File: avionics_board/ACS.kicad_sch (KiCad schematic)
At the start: 5 parts, among them J1 Conn_02x02_Odd_Even, J2 Conn_02x02_Odd_Even, J3 Conn_02x02_Odd_Even, J4 Conn_02x02_Odd_Even

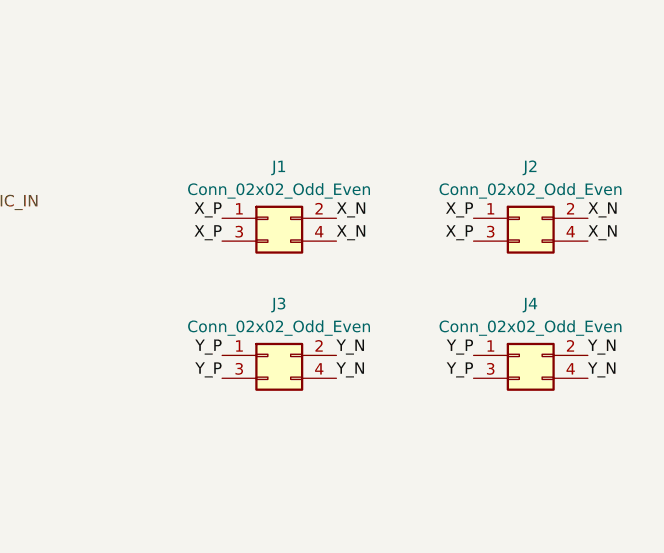
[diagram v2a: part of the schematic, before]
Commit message: AVI: using through hole M50 connectors for sun detectors and ACS
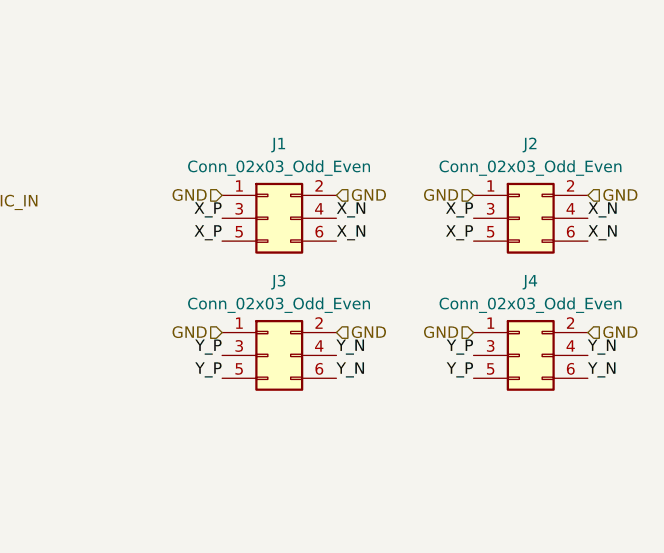
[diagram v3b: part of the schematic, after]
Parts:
- J1, J2, J3, J4: value Conn_02x02_Odd_Even -> Conn_02x03_Odd_Even; footprint Common:SAMTEC-CLP-102-02-X-DH -> Common:HARWIN_M50-3200345; symbol Connector_Generic:Conn_02x02_Odd_Even -> Connector_Generic:Conn_02x03_Odd_Even; Manufacturer (none) -> Harwin; Part Number (none) -> M50-3200345
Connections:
- net GND: now also J1.1 (Pin_1), J1.2 (Pin_2), J2.1 (Pin_1), J2.2 (Pin_2), J3.1 (Pin_1), J3.2 (Pin_2), J4.1 (Pin_1), J4.2 (Pin_2)
- net X_N: now also J1.6 (Pin_6), J2.6 (Pin_6); no longer J1.2 (Pin_2), J2.2 (Pin_2)
- net X_P: now also J1.5 (Pin_5), J2.5 (Pin_5); no longer J1.1 (Pin_1), J2.1 (Pin_1)
- net Y_N: now also J3.6 (Pin_6), J4.6 (Pin_6); no longer J3.2 (Pin_2), J4.2 (Pin_2)
- net Y_P: now also J3.5 (Pin_5), J4.5 (Pin_5); no longer J3.1 (Pin_1), J4.1 (Pin_1)
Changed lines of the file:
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@@
+		)
+	)
+	(hierarchical_label "GND"
+		(shape input)
+		(at 164.465 60.325 0)
+		(fields_autoplaced yes)
+		(effects
+			(font
+				(size 1.27 1.27)
+			)
+			(justify left)
 		)
 	)
@@
 		)
 	)
+	(hierarchical_label "GND"
+		(shape input)
+		(at 192.405 75.565 0)
+		(fields_autoplaced yes)
+		(effects
+			(font
+				(size 1.27 1.27)
+			)
+			(justify left)
+		)
+	)
 	(hierarchical_label "PWR_LOGIC_IN"
 		(shape input)
@@
 	(hierarchical_label "GND"
 		(shape input)
+		(at 151.765 75.565 180)
+		(fields_autoplaced yes)
+		(effects
+			(font
+				(size 1.27 1.27)
+			)
+			(justify right)
+		)
+	)
+	(hierarchical_label "GND"
+		(shape input)
+		(at 151.765 60.325 180)
+		(fields_autoplaced yes)
+		(effects
+			(font
+				(size 1.27 1.27)
+			)
+			(justify right)
+		)
+	)
+	(hierarchical_label "GND"
+		(shape input)
 		(at 71.12 71.755 180)
 		(fields_autoplaced yes)
@@
 		)
 	)
+	(hierarchical_label "GND"
+		(shape input)
+		(at 179.705 60.325 180)
+		(fields_autoplaced yes)
+		(effects
+			(font
+				(size 1.27 1.27)
+			)
+			(justify right)
+		)
+	)
 	(hierarchical_label "Z_PH"
 		(shape input)
@@
 		)
 	)
+	(hierarchical_label "GND"
+		(shape input)
+		(at 179.705 75.565 180)
+		(fields_autoplaced yes)
+		(effects
+			(font
+				(size 1.27 1.27)
+			)
+			(justify right)
+		)
+	)
 	(hierarchical_label "*ACS_INT"
 		(shape input)
@@
 		)
 	)
+	(hierarchical_label "GND"
+		(shape input)
+		(at 164.465 75.565 0)
+		(fields_autoplaced yes)
+		(effects
+			(font
+				(size 1.27 1.27)
+			)
+			(justify left)
+		)
+	)
 	(hierarchical_label "PWR_COIL_IN"
 		(shape input)
@@
 	(hierarchical_label "GND"
 		(shape input)
+		(at 192.405 60.325 0)
+		(fields_autoplaced yes)
+		(effects
+			(font
+				(size 1.27 1.27)
+			)
+			(justify left)
+		)
+	)
+	(hierarchical_label "GND"
+		(shape input)
 		(at 71.12 157.48 180)
 		(fields_autoplaced yes)
@@
 	)
 	(symbol
-		(lib_id "Connector_Generic:Conn_02x02_Odd_Even")
+		(lib_id "Connector_Generic:Conn_02x03_Odd_Even")
 		(at 156.845 78.105 0)
 		(unit 1)
@@
 		(fields_autoplaced yes)
 		(property "Reference" "J3"
+			(at 158.115 69.85 0)
+			(effects
+				(font
+					(size 1.27 1.27)
+				)
+			)
+		)
+		(property "Value" "Conn_02x03_Odd_Even"
 			(at 158.115 72.39 0)
 			(effects
@@
 			)
 		)
-		(property "Value" "Conn_02x02_Odd_Even"
-			(at 158.115 74.93 0)
-			(effects
-				(font
-					(size 1.27 1.27)
-				)
-			)
-		)
-		(property "Footprint" "Common:SAMTEC-CLP-102-02-X-DH"
+		(property "Footprint" "Common:HARWIN_M50-3200345"
 			(at 156.845 78.105 0)
 			(effects
@@
 			)
 		)
-		(property "Datasheet" "~"
+		(property "Datasheet" "https://cdn.harwin.com/pdfs/M50-320.pdf"
 			(at 156.845 78.105 0)
 			(effects
@@
 			)
 		)
-		(property "Description" "Generic connector, double row, 02x02, odd/even pin numbering scheme (row 1 odd numbers, row 2 even numbers), script generated (kicad-library-utils/schlib/autogen/connector/)"
+		(property "Description" "Generic connector, double row, 02x03, odd/even pin numbering scheme (row 1 odd numbers, row 2 even numbers), script generated (kicad-library-utils/schlib/autogen/connector/)"
 			(at 156.845 78.105 0)
 			(effects
@@
 			)
 		)
+		(property "Manufacturer" "Harwin"
+			(at 156.845 78.105 0)
+			(effects
+				(font
+					(size 1.27 1.27)
+				)
+				(hide yes)
+			)
+		)
+		(property "Part Number" "M50-3200345"
+			(at 156.845 78.105 0)
+			(effects
+				(font
+					(size 1.27 1.27)
+				)
+				(hide yes)
+			)
+		)
 		(pin "2"
 		)
@@
 		)
 		(pin "4"
+		)
+		(pin "5"
+		)
+		(pin "6"
 		)
 		(instances
@@
 	)
 	(symbol
-		(lib_id "Connector_Generic:Conn_02x02_Odd_Even")
+		(lib_id "Connector_Generic:Conn_02x03_Odd_Even")
 		(at 156.845 62.865 0)
 		(unit 1)
@@
 		(fields_autoplaced yes)
 		(property "Reference" "J1"
+			(at 158.115 54.61 0)
+			(effects
+				(font
+					(size 1.27 1.27)
+				)
+			)
+		)
+		(property "Value" "Conn_02x03_Odd_Even"
 			(at 158.115 57.15 0)
 			(effects
@@
 			)
 		)
-		(property "Value" "Conn_02x02_Odd_Even"
-			(at 158.115 59.69 0)
-			(effects
-				(font
-					(size 1.27 1.27)
-				)
-			)
-		)
-		(property "Footprint" "Common:SAMTEC-CLP-102-02-X-DH"
+		(property "Footprint" "Common:HARWIN_M50-3200345"
 			(at 156.845 62.865 0)
 			(effects
@@
 			)
 		)
-		(property "Datasheet" "~"
+		(property "Datasheet" "https://cdn.harwin.com/pdfs/M50-320.pdf"
 			(at 156.845 62.865 0)
 			(effects
@@
 			)
 		)
-		(property "Description" "Generic connector, double row, 02x02, odd/even pin numbering scheme (row 1 odd numbers, row 2 even numbers), script generated (kicad-library-utils/schlib/autogen/connector/)"
+		(property "Description" "Generic connector, double row, 02x03, odd/even pin numbering scheme (row 1 odd numbers, row 2 even numbers), script generated (kicad-library-utils/schlib/autogen/connector/)"
 			(at 156.845 62.865 0)
 			(effects
@@
 			)
 		)
+		(property "Manufacturer" "Harwin"
+			(at 156.845 62.865 0)
+			(effects
+				(font
+					(size 1.27 1.27)
+				)
+				(hide yes)
+			)
+		)
+		(property "Part Number" "M50-3200345"
+			(at 156.845 62.865 0)
+			(effects
+				(font
+					(size 1.27 1.27)
+				)
+				(hide yes)
+			)
+		)
 		(pin "2"
 		)
@@
 		)
 		(pin "4"
+		)
+		(pin "6"
+		)
+		(pin "5"
 		)
 		(instances
@@
 	)
 	(symbol
-		(lib_id "Connector_Generic:Conn_02x02_Odd_Even")
+		(lib_id "Connector_Generic:Conn_02x03_Odd_Even")
 		(at 184.785 62.865 0)
 		(unit 1)
@@
 		(fields_autoplaced yes)
 		(property "Reference" "J2"
+			(at 186.055 54.61 0)
+			(effects
+				(font
+					(size 1.27 1.27)
+				)
+			)
+		)
+		(property "Value" "Conn_02x03_Odd_Even"
 			(at 186.055 57.15 0)
 			(effects
@@
 			)
 		)
-		(property "Value" "Conn_02x02_Odd_Even"
-			(at 186.055 59.69 0)
-			(effects
-				(font
-					(size 1.27 1.27)
-				)
-			)
-		)
-		(property "Footprint" "Common:SAMTEC-CLP-102-02-X-DH"
+		(property "Footprint" "Common:HARWIN_M50-3200345"
 			(at 184.785 62.865 0)
 			(effects
@@
 			)
 		)
-		(property "Datasheet" "~"
+		(property "Datasheet" "https://cdn.harwin.com/pdfs/M50-320.pdf"
 			(at 184.785 62.865 0)
 			(effects
@@
 			)
 		)
-		(property "Description" "Generic connector, double row, 02x02, odd/even pin numbering scheme (row 1 odd numbers, row 2 even numbers), script generated (kicad-library-utils/schlib/autogen/connector/)"
+		(property "Description" "Generic connector, double row, 02x03, odd/even pin numbering scheme (row 1 odd numbers, row 2 even numbers), script generated (kicad-library-utils/schlib/autogen/connector/)"
 			(at 184.785 62.865 0)
 			(effects
@@
 			)
 		)
+		(property "Manufacturer" "Harwin"
+			(at 184.785 62.865 0)
+			(effects
+				(font
+					(size 1.27 1.27)
+				)
+				(hide yes)
+			)
+		)
+		(property "Part Number" "M50-3200345"
+			(at 184.785 62.865 0)
+			(effects
+				(font
+					(size 1.27 1.27)
+				)
+				(hide yes)
+			)
+		)
 		(pin "2"
 		)
@@
 		)
 		(pin "4"
+		)
+		(pin "5"
+		)
+		(pin "6"
 		)
 		(instances
@@
 	)
 	(symbol
-		(lib_id "Connector_Generic:Conn_02x02_Odd_Even")
+		(lib_id "Connector_Generic:Conn_02x03_Odd_Even")
 		(at 184.785 78.105 0)
 		(unit 1)
@@
 		(fields_autoplaced yes)
 		(property "Reference" "J4"
+			(at 186.055 69.85 0)
+			(effects
+				(font
+					(size 1.27 1.27)
+				)
+			)
+		)
+		(property "Value" "Conn_02x03_Odd_Even"
 			(at 186.055 72.39 0)
 			(effects
@@
 			)
 		)
-		(property "Value" "Conn_02x02_Odd_Even"
-			(at 186.055 74.93 0)
-			(effects
-				(font
-					(size 1.27 1.27)
-				)
-			)
-		)
-		(property "Footprint" "Common:SAMTEC-CLP-102-02-X-DH"
+		(property "Footprint" "Common:HARWIN_M50-3200345"
 			(at 184.785 78.105 0)
 			(effects
@@
 			)
 		)
-		(property "Datasheet" "~"
+		(property "Datasheet" "https://cdn.harwin.com/pdfs/M50-320.pdf"
 			(at 184.785 78.105 0)
 			(effects
@@
 			)
 		)
-		(property "Description" "Generic connector, double row, 02x02, odd/even pin numbering scheme (row 1 odd numbers, row 2 even numbers), script generated (kicad-library-utils/schlib/autogen/connector/)"
+		(property "Description" "Generic connector, double row, 02x03, odd/even pin numbering scheme (row 1 odd numbers, row 2 even numbers), script generated (kicad-library-utils/schlib/autogen/connector/)"
 			(at 184.785 78.105 0)
 			(effects
@@
 			)
 		)
+		(property "Manufacturer" "Harwin"
+			(at 184.785 78.105 0)
+			(effects
+				(font
+					(size 1.27 1.27)
+				)
+				(hide yes)
+			)
+		)
+		(property "Part Number" "M50-3200345"
+			(at 184.785 78.105 0)
+			(effects
+				(font
+					(size 1.27 1.27)
+				)
+				(hide yes)
+			)
+		)
 		(pin "2"
 		)
@@
 		(pin "4"
 		)
+		(pin "5"
+		)
+		(pin "6"
+		)
 		(instances

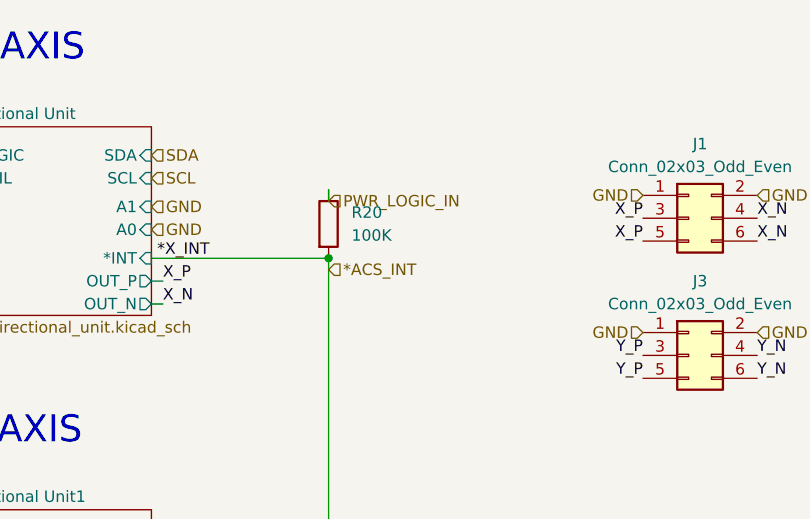
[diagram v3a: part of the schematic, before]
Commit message: QC, add second 3V regulator to AUX, INT pullups on AUX SCI AVI
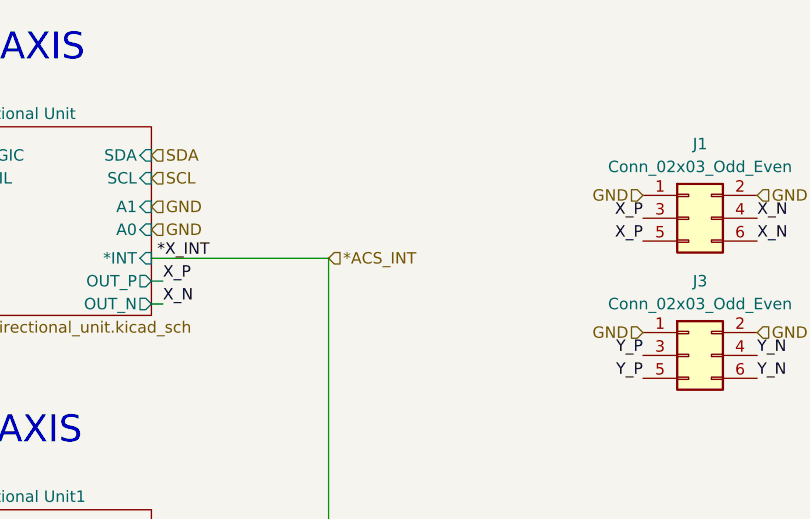
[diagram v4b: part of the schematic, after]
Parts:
- removed R20: 100K, Resistor_SMD:R_0402_1005Metric_Pad0.72x0.64mm_HandSolder, symbol Device:R
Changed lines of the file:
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@@
 		(color 0 0 0 0)
 	)
-	(junction
-		(at 116.84 67.31)
-		(diameter 0)
-		(color 0 0 0 0)
-	)
 	(wire
 		(pts
@@
 	(wire
 		(pts
-			(xy 116.84 59.69) (xy 116.84 60.96)
-		)
-		(stroke
-			(width 0)
-			(type default)
-		)
-	)
-	(wire
-		(pts
 			(xy 98.425 72.39) (xy 97.155 72.39)
 		)
@@
 	(wire
 		(pts
+			(xy 116.84 67.31) (xy 116.84 109.855)
+		)
+		(stroke
+			(width 0)
+			(type default)
+		)
+	)
+	(wire
+		(pts
 			(xy 98.425 69.85) (xy 97.155 69.85)
-		)
-		(stroke
-			(width 0)
-			(type default)
-		)
-	)
-	(wire
-		(pts
-			(xy 116.84 67.31) (xy 116.84 109.855)
 		)
 		(stroke
@@
 	(hierarchical_label "*ACS_INT"
 		(shape input)
-		(at 116.84 68.58 0)
+		(at 116.84 67.31 0)
 		(fields_autoplaced yes)
 		(effects
@@
 			)
 			(justify right)
-		)
-	)
-	(hierarchical_label "PWR_LOGIC_IN"
-		(shape input)
-		(at 116.84 60.96 0)
-		(fields_autoplaced yes)
-		(effects
-			(font
-				(size 1.27 1.27)
-			)
-			(justify left)
 		)
 	)
@@
 					(unit 1)
 				)
-			)
-		)
-	)
-	(symbol
-		(lib_id "Device:R")
-		(at 116.84 63.5 0)
-		(unit 1)
-		(exclude_from_sim no)
-		(in_bom yes)
-		(on_board yes)
-		(dnp no)
-		(fields_autoplaced yes)
-		(property "Reference" "R20"
-			(at 119.38 62.2299 0)
-			(effects
-				(font
-					(size 1.27 1.27)
-				)
-				(justify left)
-			)
-		)
-		(property "Value" "100K"
-			(at 119.38 64.7699 0)
-			(effects
-				(font
-					(size 1.27 1.27)
-				)
-				(justify left)
-			)
-		)
-		(property "Footprint" "Resistor_SMD:R_0402_1005Metric_Pad0.72x0.64mm_HandSolder"
-			(at 115.062 63.5 90)
-			(effects
-				(font
-					(size 1.27 1.27)
-				)
-				(hide yes)
-			)
-		)
-		(property "Datasheet" "https://www.yageo.com/upload/media/product/products/datasheet/rchip/PYu-RC_Group_51_RoHS_L_12.pdf"
-			(at 116.84 63.5 0)
-			(effects
-				(font
-					(size 1.27 1.27)
-				)
-				(hide yes)
-			)
-		)
-		(property "Description" "Resistor"
-			(at 116.84 63.5 0)
-			(effects
-				(font
-					(size 1.27 1.27)
-				)
-				(hide yes)
-			)
-		)
-		(property "Alt" ""
-			(at 116.84 63.5 0)
-			(effects
-				(font
-					(size 1.27 1.27)
-				)
-				(hide yes)
-			)
-		)
-		(property "Manufacturer" "YAGEO"
-			(at 116.84 63.5 0)
-			(effects
-				(font
-					(size 1.27 1.27)
-				)
-				(hide yes)
-			)
-		)
-		(property "Part Number" "RC0402FR-07100KL"
-			(at 116.84 63.5 0)
-			(effects
-				(font
-					(size 1.27 1.27)
-				)
-				(hide yes)
-			)
-		)
-		(property "Tolerance" "1"
-			(at 116.84 63.5 0)
-			(effects
-				(font
-					(size 1.27 1.27)
-				)
-				(hide yes)
-			)
-		)
-		(pin "1"
-		)
-		(pin "2"
-		)
-		(instances
-			(project "AVIONICS_BOARD"
-				(path "/f6cc00ab-17f1-4973-862f-7ac95fe70668/1f9ae17d-3f3e-4633-9b01-30c344473415"
-					(reference "R20")
-					(unit 1)
-				)
